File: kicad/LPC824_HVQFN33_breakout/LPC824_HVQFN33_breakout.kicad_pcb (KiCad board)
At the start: 2 copper layers, 2 parts, among them M1 LPC824M201JHI33

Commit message: * updated LPC824 breakout
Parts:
- added J1: PINS_2X09, SquantorConnectors:Header-0254-2X09-H010, F.Cu at (145.5, 104.6)
- added J2: PINS_2X09, SquantorConnectors:Header-0254-2X09-H010, F.Cu at (166.5, 104.0)
- turned M1 to 315 degrees
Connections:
- C1 pad 1: (no net) -> /VCC
- M1 pad 1: (no net) -> /PIO0_13
- M1 pad 10: (no net) -> /PIO0_16
- M1 pad 11: (no net) -> /PIO0_27
- M1 pad 12: (no net) -> /PIO0_26
- M1 pad 13: (no net) -> /PIO0_25
- M1 pad 14: (no net) -> /PIO0_24
- M1 pad 15: (no net) -> /PIO0_15
- M1 pad 16: (no net) -> /PIO0_1
- M1 pad 17: (no net) -> /PIO0_9
- M1 pad 18: (no net) -> /PIO0_8
- M1 pad 19: (no net) -> /VCC
- M1 pad 2: (no net) -> /PIO0_12
- M1 pad 20: (no net) -> /AGND
- M1 pad 21: (no net) -> /AREF
- M1 pad 3: (no net) -> /PIO0_5
- M1 pad 4: (no net) -> /PIO0_4
- M1 pad 5: (no net) -> /PIO0_28
- M1 pad 6: (no net) -> /PIO0_3
- M1 pad 7: (no net) -> /PIO0_2
- M1 pad 8: (no net) -> /PIO0_11
- M1 pad 9: (no net) -> /PIO0_10

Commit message: * fully connected up connectors - next JTAG connection
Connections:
- J1 pad 1: /PIO0_13 -> /PIO0_12
- J1 pad 2: /PIO0_12 -> /PIO0_13
- J1 pad 3: /PIO0_5 -> /PIO0_4
- J1 pad 4: /PIO0_4 -> /PIO0_5
- J1 pad 5: /PIO0_28 -> /PIO0_3
- J1 pad 6: /PIO0_3 -> /PIO0_28
- J1 pad 7: /PIO0_2 -> /PIO0_11
- J1 pad 8: /PIO0_11 -> /PIO0_2
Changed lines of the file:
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@@
     (fp_line (start 9.525 2.54) (end 10.795 2.54) (layer F.SilkS) (width 0.1524))
     (pad 1 thru_hole rect (at -10.16 1.27 270) (size 1.3 1.3) (drill 1) (layers *.Cu *.Mask)
+      (net 4 /PIO0_12))
+    (pad 2 thru_hole circle (at -10.16 -1.27 270) (size 1.3 1.3) (drill 1) (layers *.Cu *.Mask)
       (net 3 /PIO0_13))
-    (pad 2 thru_hole circle (at -10.16 -1.27 270) (size 1.3 1.3) (drill 1) (layers *.Cu *.Mask)
-      (net 4 /PIO0_12))
     (pad 3 thru_hole circle (at -7.62 1.27 270) (size 1.3 1.3) (drill 1) (layers *.Cu *.Mask)
+      (net 6 /PIO0_4))
+    (pad 4 thru_hole circle (at -7.62 -1.27 270) (size 1.3 1.3) (drill 1) (layers *.Cu *.Mask)
       (net 5 /PIO0_5))
-    (pad 4 thru_hole circle (at -7.62 -1.27 270) (size 1.3 1.3) (drill 1) (layers *.Cu *.Mask)
-      (net 6 /PIO0_4))
     (pad 5 thru_hole circle (at -5.08 1.27 270) (size 1.3 1.3) (drill 1) (layers *.Cu *.Mask)
+      (net 8 /PIO0_3))
+    (pad 6 thru_hole circle (at -5.08 -1.27 270) (size 1.3 1.3) (drill 1) (layers *.Cu *.Mask)
       (net 7 /PIO0_28))
-    (pad 6 thru_hole circle (at -5.08 -1.27 270) (size 1.3 1.3) (drill 1) (layers *.Cu *.Mask)
-      (net 8 /PIO0_3))
     (pad 7 thru_hole circle (at -2.54 1.27 270) (size 1.3 1.3) (drill 1) (layers *.Cu *.Mask)
+      (net 10 /PIO0_11))
+    (pad 8 thru_hole circle (at -2.54 -1.27 270) (size 1.3 1.3) (drill 1) (layers *.Cu *.Mask)
       (net 9 /PIO0_2))
-    (pad 8 thru_hole circle (at -2.54 -1.27 270) (size 1.3 1.3) (drill 1) (layers *.Cu *.Mask)
-      (net 10 /PIO0_11))
     (pad 9 thru_hole circle (at 0 1.27 270) (size 1.3 1.3) (drill 1) (layers *.Cu *.Mask)
       (net 11 /PIO0_10))

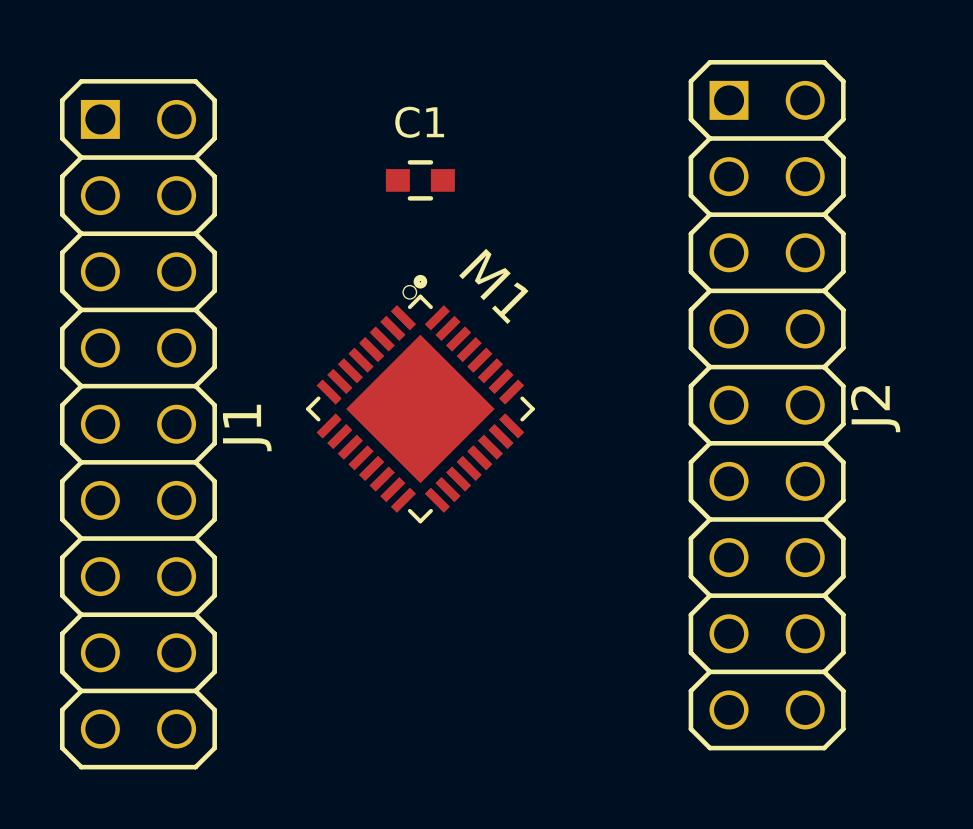
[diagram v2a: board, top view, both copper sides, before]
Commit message: * further layout of the LPC824 chip
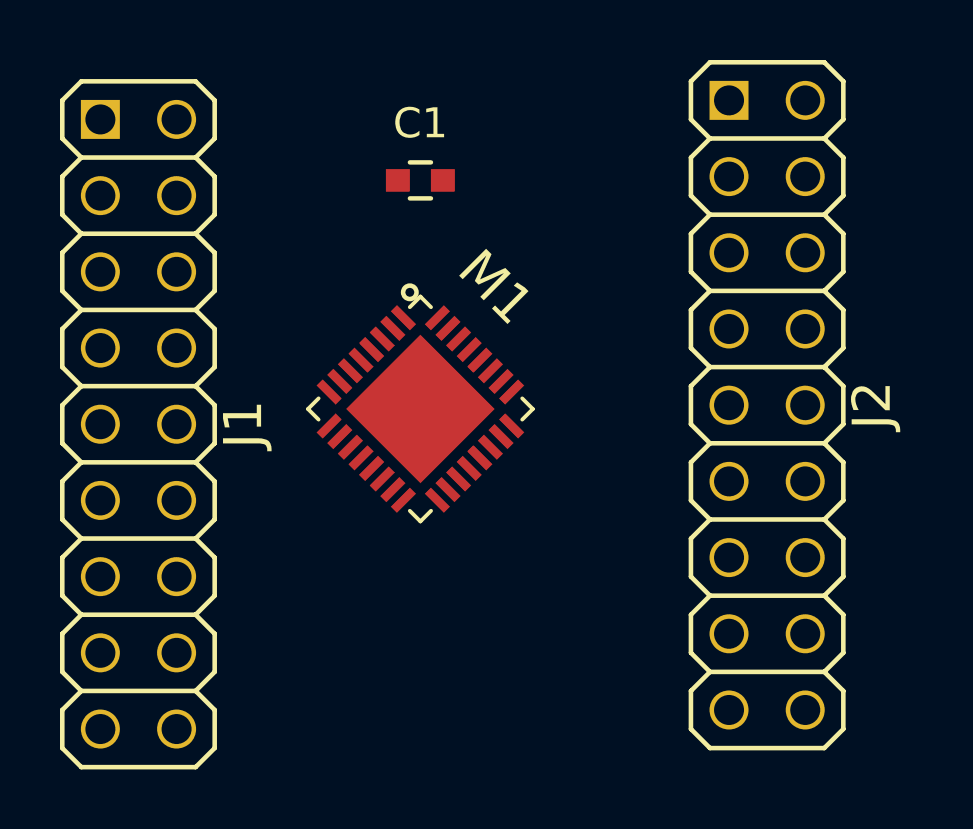
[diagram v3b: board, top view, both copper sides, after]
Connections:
- J1 pad 10: /PIO0_16 -> /PIO0_10
- J1 pad 11: /PIO0_27 -> /PIO0_26
- J1 pad 12: /PIO0_26 -> /PIO0_27
- J1 pad 13: /PIO0_25 -> /PIO0_24
- J1 pad 14: /PIO0_24 -> /PIO0_25
- J1 pad 15: /PIO0_15 -> /PIO0_1
- J1 pad 16: /PIO0_1 -> /PIO0_15
- J1 pad 9: /PIO0_10 -> /PIO0_16
- J2 pad 1: (no net) -> /PIO0_17
- J2 pad 2: (no net) -> /PIO0_18
- J2 pad 3: (no net) -> /PIO0_19
- J2 pad 4: (no net) -> /PIO0_20
- M1 pad 29: (no net) -> /PIO0_20
- M1 pad 30: (no net) -> /PIO0_19
- M1 pad 31: (no net) -> /PIO0_18
- M1 pad 32: (no net) -> /PIO0_17
